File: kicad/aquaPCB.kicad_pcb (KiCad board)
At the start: 2 copper layers, 100 x 100 mm, 149 parts, among them J1 12V IN, J11 SSR G17, J12 SSR G22, J13 SSR G23, J14 SSR G27, J15 IN1, J16 IN2, J17 IN3, J18 IN4, J19 1-Wire 1, J2 Raspberry Pi, J22 I2C 1, J23 I2C 2, J24 Display, J25 pH probe, J26 Module, J27 AIN3, J4 OUT G18, J5 OUT G19, J6 OUT G12, J7 OUT G13, J8 OUT G16, J9 OUT G26, Q1 AOD4184A, Q10 AOD4185, Q2 AOD4184A, Q3 AOD4184A, Q4 AOD4184A, Q5 AOD4184A, Q6 AOD4184A, U1 TPS54360B, U2 AMS1117-3.3, U3 74HCT244D, U4 ULN2803A, U5 ADS1115IDGSR, U6 TLV9062IDR

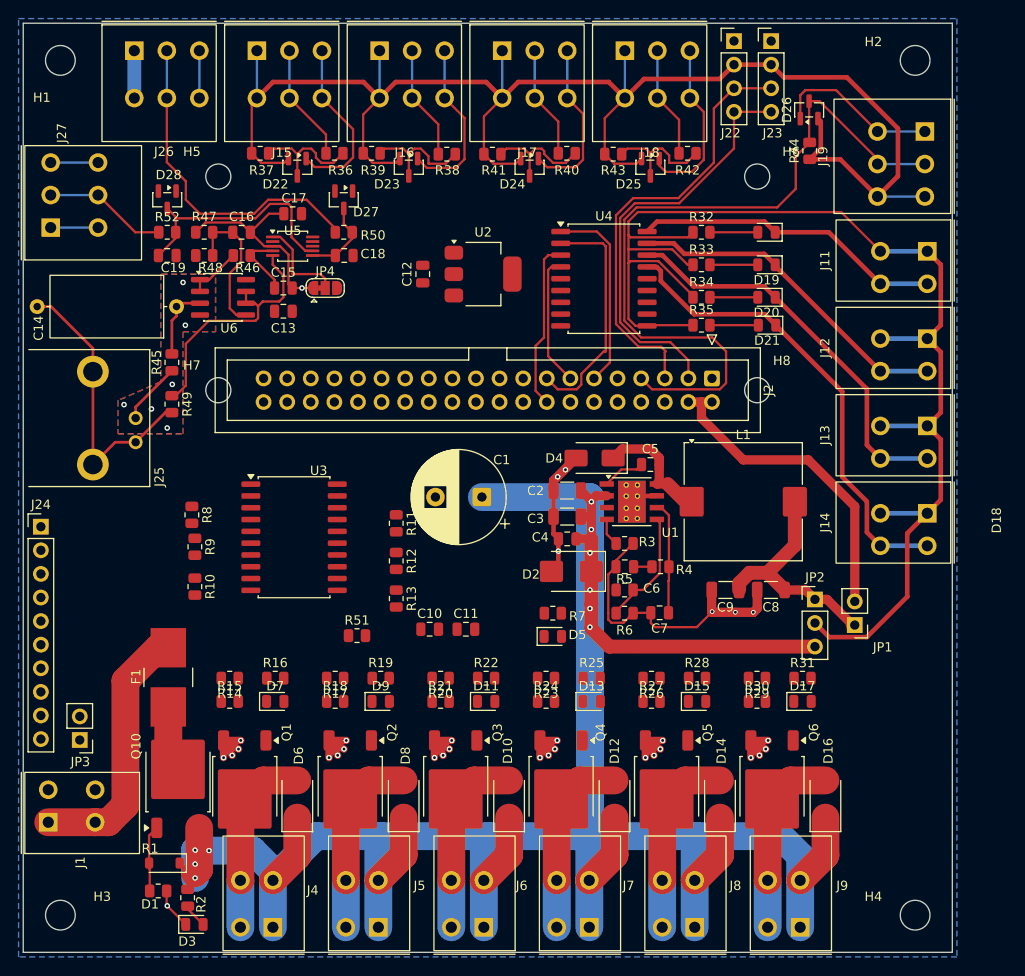
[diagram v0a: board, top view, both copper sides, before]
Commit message: kicad: routing progress (by hand)
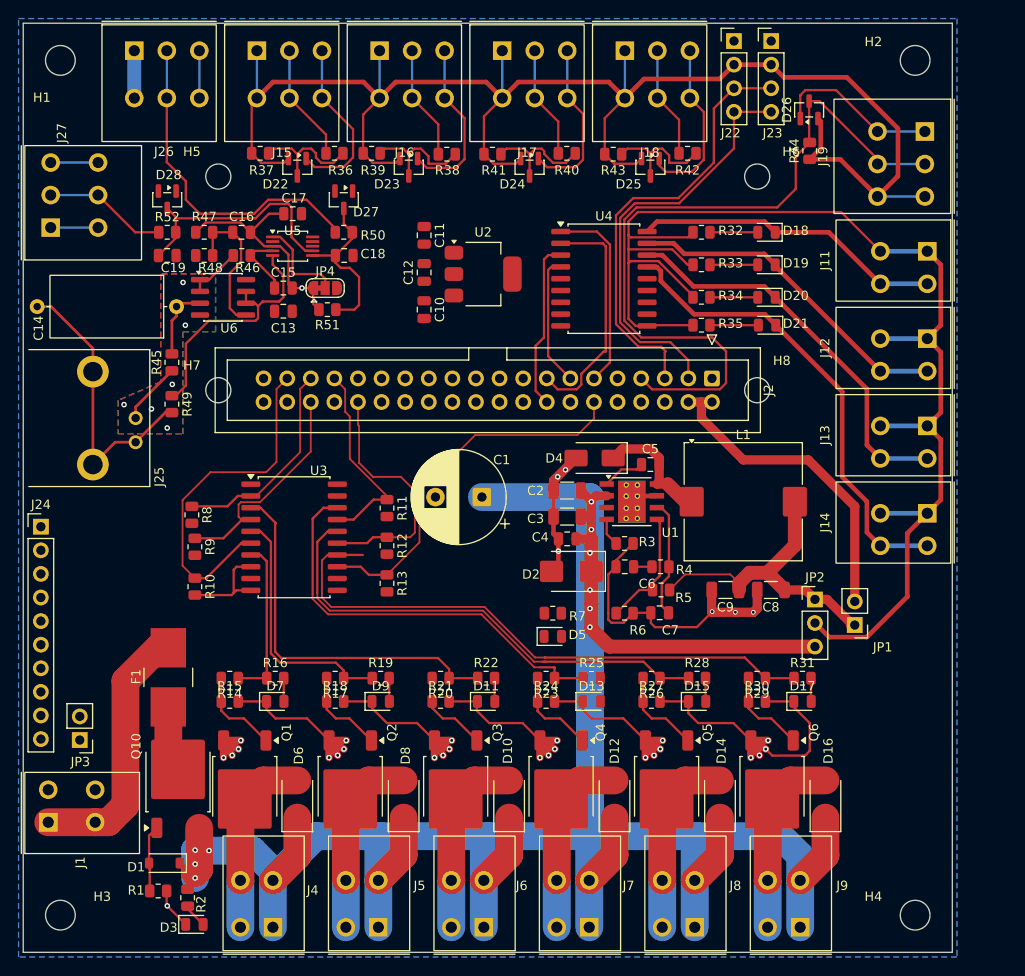
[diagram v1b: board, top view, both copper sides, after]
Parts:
- moved C11 42.6 mm to (122.0, 58.5), turned to -90 degrees
- moved R51 35.2 mm to (111.6, 66.5), turned to 180 degrees
- moved C10 34.4 mm to (122.0, 66.5), turned to -90 degrees
- moved R5 3.93 mm to (147.5, 96.7), turned to 180 degrees
- moved R11 1.92 mm to (118.0, 87.9)
- moved R12 1.92 mm to (118.0, 91.9)
- moved R13 1.92 mm to (118.0, 96.0)
- moved C12 0.23 mm to (122.0, 62.5)
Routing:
- net GND: track 221.5 -> 309.6 mm
- net /Power outputs Q1..Q6/Q6_DRV: track 0.00 -> 63.1 mm
- net /Power outputs Q1..Q6/Q5_DRV: track 0.00 -> 52.5 mm
- net /Power outputs Q1..Q6/Q4_DRV: track 0.00 -> 45.1 mm
- net /Power outputs Q1..Q6/Q3_DRV: track 0.00 -> 40.8 mm
- net GPIO18_Q1: track 0.00 -> 40.0 mm
- net GPIO26_Q6: track 0.00 -> 37.8 mm
- net GPIO12_Q2: track 0.00 -> 27.2 mm
- net /Power outputs Q1..Q6/Q2_DRV: track 0.00 -> 27.1 mm
- net GPIO16_Q5: track 0.00 -> 25.1 mm
- net GPIO19_Q4: track 0.00 -> 22.5 mm
- net GPIO13_Q3: track 0.00 -> 21.6 mm
- net /Power outputs Q1..Q6/Q1_DRV: track 0.00 -> 17.8 mm
- net /ADS1115 ADC and pH amplifier/AIN2: track 8.66 -> 18.3 mm
- net /Power outputs Q1..Q6/Q4_G: track 0.00 -> 9.66 mm
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
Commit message: kicad: routing progress (by hand)
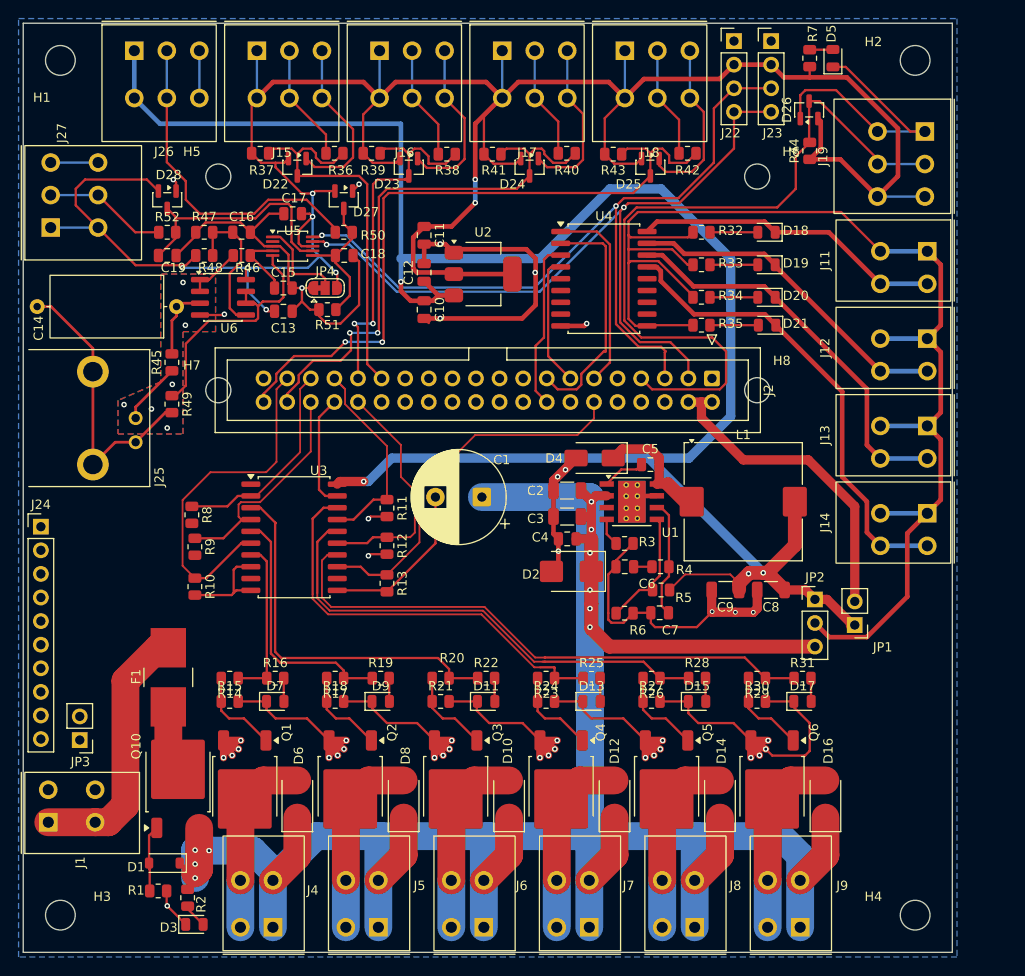
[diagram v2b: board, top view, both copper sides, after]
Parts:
- moved D5 69.2 mm to (166.0, 39.4), turned to 90 degrees
- moved R7 65.8 mm to (163.5, 39.4), turned to 90 degrees
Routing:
- net +5V: track 38.5 -> 216.4 mm, vias 0 -> 4
- net +3V3: track 175.9 -> 288.5 mm, vias 0 -> 8
- net GND: track 309.6 -> 415.9 mm, vias 32 -> 41
- net GPIO21_IN4: track 12.6 -> 74.3 mm, vias 0 -> 2
- net GPIO20_IN3: track 12.3 -> 59.2 mm, vias 0 -> 2
- net GPIO2_SDA: track 45.5 -> 85.4 mm, vias 0 -> 2
- net GPIO3_SCL: track 47.0 -> 86.1 mm, vias 0 -> 2
- net GPIO5_IN1: track 12.4 -> 41.8 mm
- net GPIO6_IN2: track 12.7 -> 40.0 mm, vias 0 -> 2
- net /Power outputs Q1..Q6/Q6_DRV: track 63.1 -> 60.4 mm
- net /ADS1115 ADC and pH amplifier/AIN2: track 18.3 -> 15.7 mm
- net /Power outputs Q1..Q6/Q4_LED: track 0.00 -> 2.51 mm
- net Net-(D5-A): track 0.00 -> 2.51 mm
- net /Power outputs Q1..Q6/Q3_G: track 6.96 -> 9.46 mm
- net GPIO12_Q2: track 27.2 -> 25.4 mm
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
